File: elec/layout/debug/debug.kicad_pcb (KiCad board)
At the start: 2 copper layers, 100 x 100 mm, 100 parts

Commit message: merge
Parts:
- added C32: 10V 4.7uF X5R ±20% 0402 Multilayer Ceramic Capacitors MLCC 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, lib:C0402, F.Cu at (154.7, 68.9)
- added C33: 16V 100nF X7R ±10% 0402 Multilayer Ceramic Capacitors MLCC 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, lib:C0402, F.Cu at (163.1, 71.5)
- added C34: 25V 1uF X5R ±10% 0402 Multilayer Ceramic Capacitors MLCC - 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, lib:C0402, F.Cu at (154.7, 66.4)
- added C35: 16V 100nF X7R ±10% 0402 Multilayer Ceramic Capacitors MLCC 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, lib:C0402, F.Cu at (163.0, 70.4)
- added C36: 50V 10nF X7R ±10% 0402 Multilayer Ceramic Capacitors MLCC -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, lib:C0402, F.Cu at (154.7, 65.5)
- added C37: 50V 13pF C0G ±2% 0402 Multilayer Ceramic Capacitors MLCC - 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, lib:C0402, F.Cu at (156.3, 73.2)
- added C38: 50V 13pF C0G ±2% 0402 Multilayer Ceramic Capacitors MLCC - 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, lib:C0402, F.Cu at (154.7, 69.9)
- added C39: 50V 11pF C0G ±5% 0402 Multilayer Ceramic Capacitors MLCC - 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, lib:C0402, F.Cu at (179.4, 62.1)
- added C40: 50V 11pF C0G ±5% 0402 Multilayer Ceramic Capacitors MLCC - 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, lib:C0402, F.Cu at (174.7, 62.7)
- added C41: 10V 470nF X5R ±10% 0402 Multilayer Ceramic Capacitors MLCC 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, lib:C0402, F.Cu at (179.4, 64.1)
- added C42: 16V 100nF X7R ±10% 0402 Multilayer Ceramic Capacitors MLCC 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, lib:C0402, F.Cu at (178.3, 71.0)
- added C43: 16V 100nF X7R ±10% 0402 Multilayer Ceramic Capacitors MLCC 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, lib:C0402, F.Cu at (175.2, 68.3)
- added C44: 50V 10nF X7R ±10% 0402 Multilayer Ceramic Capacitors MLCC -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, lib:C0402, F.Cu at (175.2, 69.3)
- added C45: 50V 10nF X7R ±10% 0402 Multilayer Ceramic Capacitors MLCC -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, lib:C0402, F.Cu at (180.5, 64.1)
- added C46: 50V 1pF C0G 0402 Multilayer Ceramic Capacitors MLCC - SMD/S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, lib:C0402, F.Cu at (182.1, 68.6)
- added C47: 50V 1pF C0G 0402 Multilayer Ceramic Capacitors MLCC - SMD/S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, lib:C0402, F.Cu at (182.8, 65.7)
- added C48: 50V 1pF C0G 0402 Multilayer Ceramic Capacitors MLCC - SMD/S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, lib:C0402, F.Cu at (185.6, 65.7)
- added C49: 50V 1pF C0G 0402 Multilayer Ceramic Capacitors MLCC - SMD/S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, lib:C0402, F.Cu at (184.2, 66.2)
- added C50: 50V 100pF C0G ±5% 0402 Multilayer Ceramic Capacitors MLCC -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, lib:C0402, F.Cu at (186.0, 67.1)
- added L2: , lib:L0402, F.Cu at (182.3, 67.2)
- added L3: , lib:L0402, F.Cu at (184.2, 67.2)
- added R16: 62.5mW Thick Film Resistors ±100ppm/℃ ±1% 330Ω 0402 Chip Re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, lib:R0402, F.Cu at (158.8, 64.1)
- added R17: 62.5mW Thick Film Resistors ±100ppm/℃ ±1% 10kΩ 0402 Chip Re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, lib:R0402, F.Cu at (157.2, 64.1)
- added U12: , lib:UFQFPN-32_L5.0-W5.0-P0.50-TL-EP3.5, F.Cu at (158.9, 68.5)
- added U13: , lib:FC-135R_L3.2-W1.5, F.Cu at (154.5, 72.4)
- added U14: , lib:QFN-24_L4.0-W4.0-P0.50-BL-EP2.6, F.Cu at (178.7, 67.4)
- added U15: , lib:OSC-SMD_4P-L2.0-W1.6-BL, F.Cu at (177.0, 62.7)
- added U16: , lib:IPEX-SMD_BWIPX-1-001E, F.Cu at (188.5, 67.1)
- added U17: , lib:HDR-SMD_10P-P1.27-V-M-R2-C5-LS5.3, F.Cu at (164.6, 58.2)
- renumbered C32 to C51, C33 to C52, C34 to C53, C35 to C54, R16 to R18, R17 to R19, R18 to R20, R19 to R21, R20 to R22, R21 to R23, R22 to R24, R23 to R25, R24 to R26, R25 to R27, R26 to R28, R27 to R29, R28 to R30, R29 to R31, R30 to R32, R31 to R33, R32 to R34, R33 to R35, R34 to R36, R35 to R37, R36 to R38, R37 to R39, R38 to R40, U12 to U18, U13 to U19, U14 to U20, U15 to U21, U16 to U22, U17 to U23, U18 to U24, U19 to U25, U20 to U26, U21 to U27, U22 to U28, U23 to U29, U24 to U30
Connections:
- net vcc-13 renamed vcc-19
- net vcc-14 renamed vcc-20
- net vcc-15 renamed vcc-21
- net vcc-16 renamed vcc-22
- net vcc-17 renamed vcc-23
- R28 pad 2: _7 -> _7-1
- R32 pad 2: _7-1 -> _7-2
- R36 pad 2: _7-2 -> _7-3
- R40 pad 2: _7-3 -> _7-4
- U27 pad 7: _7 -> _7-1
- U28 pad 7: _7-1 -> _7-2
- U29 pad 7: _7-2 -> _7-3
- U30 pad 7: _7-3 -> _7-4
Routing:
- net gnd: track 85.0 -> 114.7 mm, vias 12 -> 20
- net gnd-5: track 1.55 -> 14.2 mm, vias 0 -> 43
- net pc14_osc32_in: track 0.00 -> 12.5 mm
- net vcc: track 102.0 -> 113.2 mm, vias 20 -> 24
- net vcc-15: track 0.00 -> 8.78 mm, vias 0 -> 2
- net pc15_osc32_out: track 0.00 -> 8.52 mm
- net preterm: track 0.00 -> 6.08 mm
- net vcc-7: track 23.4 -> 28.1 mm
- net vcc-18: track 0.00 -> 2.86 mm
- net vcc-17: track 0.00 -> 2.86 mm
- net io-3: track 0.00 -> 2.28 mm
- net _7: track 2.28 -> 0.00 mm
- net _7-4: track 0.00 -> 2.28 mm
- net ph3_boot0: track 0.00 -> 1.62 mm
- net vcc-1: track 78.4 -> 79.9 mm
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
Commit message: layout 95%
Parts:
- added C55: 25V 1uF X5R ±10% 0402 Multilayer Ceramic Capacitors MLCC - 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, lib:C0402, F.Cu at (173.8, 102.9)
- added C56: 25V 1uF X5R ±10% 0402 Multilayer Ceramic Capacitors MLCC - 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, lib:C0402, F.Cu at (175.7, 102.9)
- added R41: 62.5mW Thick Film Resistors ±100ppm/℃ ±1% 1kΩ 0402 Chip Res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, lib:R0402, F.Cu at (160.1, 83.3)
- added R42: 62.5mW Thick Film Resistors ±100ppm/℃ ±1% 1kΩ 0402 Chip Res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, lib:R0402, F.Cu at (157.5, 83.3)
- added R43: 62.5mW Thick Film Resistors ±100ppm/℃ ±1% 1kΩ 0402 Chip Res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, lib:R0402, F.Cu at (155.0, 83.3)
- added R44: 62.5mW Thick Film Resistors ±100ppm/℃ ±1% 1kΩ 0402 Chip Res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, lib:R0402, F.Cu at (152.4, 83.3)
- added R45: 62.5mW Thick Film Resistors ±100ppm/℃ ±1% 1kΩ 0402 Chip Res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, lib:R0402, F.Cu at (168.9, 61.2)
- added R46: 62.5mW Thick Film Resistors ±100ppm/℃ ±1% 1kΩ 0402 Chip Res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, lib:R0402, F.Cu at (171.4, 61.2)
- added R47: 62.5mW Thick Film Resistors ±100ppm/℃ ±1% 1kΩ 0402 Chip Res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, lib:R0402, F.Cu at (174.0, 61.2)
- added R48: 62.5mW Thick Film Resistors ±100ppm/℃ ±1% 1kΩ 0402 Chip Res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, lib:R0402, F.Cu at (176.5, 61.2)
- added U27: , lib:VSSOP-10_L3.0-W3.0-P0.50-LS4.9-BL, F.Cu at (174.9, 105.1)
- added U28: , lib:CONN-TH_DB125-2.54-2P-GN, F.Cu at (195.8, 106.0)
- added U33: , lib:HDR-SMD_8P-P2.54-V-M-R2-C4-LS7.4, F.Cu at (156.2, 88.9)
- added U34: , lib:HDR-SMD_8P-P2.54-V-M-R2-C4-LS7.4, F.Cu at (172.7, 55.6)
- moved C44 6.14 mm to (171.8, 74.4)
- moved C42 5.78 mm to (174.6, 75.4)
- moved C32 5.58 mm to (151.3, 73.4)
- moved C33 5.58 mm to (159.7, 76.0)
- moved C34 5.58 mm to (151.3, 70.9)
- moved C35 5.58 mm to (159.7, 74.9)
- moved C38 5.58 mm to (151.3, 74.4)
- moved C39 5.58 mm to (176.1, 66.6)
- moved C40 5.58 mm to (171.4, 67.1)
- moved C41 5.58 mm to (176.1, 68.6)
- moved C45 5.58 mm to (177.1, 68.6)
- moved C46 5.58 mm to (178.7, 73.1)
- moved C47 5.58 mm to (179.4, 70.2)
- moved C49 5.58 mm to (180.8, 70.7)
- moved L2 5.58 mm to (178.9, 71.6)
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- renumbered U27 to U29, U28 to U30, U29 to U31, U30 to U32
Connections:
- net vcc-20 renamed vcc-24
- C39 pad 1: xin-1 -> xta
- C40 pad 1: xout-1 -> xtb
- C41 pad 1: vcc-15 -> vcc-19
- C44 pad 1: vcc-15 -> vcc-19
- C45 pad 1: vcc-14 -> vcc-18
- C46 pad 1: io-3 -> io-1
- C47 pad 1: vcc-17 -> vcc-21
- C48 pad 1: vcc-18 -> vcc-22
- C49 pad 1: vcc-17 -> vcc-21
- C49 pad 2: vcc-18 -> vcc-22
- C50 pad 1: vcc-18 -> vcc-22
- C50 pad 2: gnd-11 -> gnd-10
- L2 pad 1: io-3 -> io-1
- L2 pad 2: vcc-17 -> vcc-21
- L3 pad 1: vcc-17 -> vcc-21
- L3 pad 2: vcc-18 -> vcc-22
- R24 pad 2: vcc-19 -> vcc-23
- R40 pad 1: vcc-23 -> vcc-28
- U12 pad 18: io -> vcc-13
- U12 pad 19: scl-1 -> vcc-14
- U12 pad 20: sda-1 -> vcc-15
- U12 pad 21: io-1 -> vcc-16
- U12 pad 27: io-2 -> io
- U14 pad 1: vcc-14 -> vcc-18
- U14 pad 10: io -> vcc-13
- U14 pad 12: vcc-15 -> vcc-19
- U14 pad 2: vcc-15 -> vcc-19
- U14 pad 22: io-3 -> io-1
- U14 pad 3: io-2 -> io
- U14 pad 7: io-1 -> vcc-16
- U14 pad 8: sda-1 -> vcc-15
- U14 pad 9: scl-1 -> vcc-14
- U15 pad 1: xin-1 -> xta
- U15 pad 2: gnd-10 -> gnd
- U15 pad 3: xout-1 -> xtb
- U15 pad 4: gnd-10 -> gnd
- U16 pad 1: gnd-11 -> gnd-10
- U17 pad 1: vcc-13 -> vcc-17
- U20 pad 2: vcc-21 -> vcc-25
- U21 pad 2: vcc-22 -> vcc-26
- U21 pad 4: vcc-21 -> vcc-25
- U26 pad 3: vcc-19 -> vcc-23
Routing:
- net vcc-2: track 50.2 -> 148.8 mm, vias 0 -> 4
- net vcc-3: track 36.0 -> 103.1 mm
- net scl: track 41.1 -> 106.5 mm, vias 4 -> 6
- net sda: track 39.9 -> 101.2 mm
- net vcc-1: track 79.9 -> 134.1 mm, vias 4 -> 6
- net gnd: track 114.7 -> 164.2 mm, vias 20 -> 23
- net dm: track 2.76 -> 51.1 mm, vias 0 -> 4
- net dp: track 2.76 -> 47.3 mm
- net mosi-1: track 0.00 -> 36.4 mm, vias 0 -> 2
- net cs-2: track 0.00 -> 35.3 mm
- net sck-2: track 0.00 -> 32.8 mm, vias 0 -> 2
- net vcc-13: track 0.00 -> 32.4 mm, vias 0 -> 2
- net miso-2: track 0.00 -> 31.3 mm, vias 0 -> 3
- net vcc-16: track 0.00 -> 30.3 mm
- net vcc-14: track 1.18 -> 31.3 mm, vias 0 -> 2
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- added copper zone on F.Cu, net gnd
- added copper zone on In1.Cu, net gnd
- added copper zone on B.Cu, net vcc
- added copper zone on In2.Cu, net vcc
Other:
- copper layers 2 -> 4

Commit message: layout complete
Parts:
- added D1: , lib:SMA_L4.2-W2.6-LS5.3-RD, F.Cu at (119.7, 75.0)
- added J1: , lib:CONN-SMD_4P-P1.00_SM04B-SRSS-TB-LF-SN, F.Cu at (195.8, 83.5)
- added R1: 62.5mW Thick Film Resistors ±100ppm/℃ ±1% 10kΩ 0402 Chip Re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, lib:R0402, F.Cu at (181.1, 96.5)
- added R2: 62.5mW Thick Film Resistors ±100ppm/℃ ±1% 10kΩ 0402 Chip Re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, lib:R0402, F.Cu at (179.0, 97.2)
- added U37: , lib:RES-ADJ-TH_RK09K1130AJ3, F.Cu at (148.8, 139.6)
- added U4: , lib:KEY-SMD_4P-L4.2-W3.2-P2.20-LS4.6, F.Cu at (149.5, 124.8)
- added U5: , lib:KEY-SMD_4P-L4.2-W3.2-P2.20-LS4.6, F.Cu at (128.9, 116.2)
- R11: renamed from R9; value 62.5mW Thick Film Resistors ±100ppm/℃ ±1% 1MΩ 0402 Chip Resistor - Surface Mount ROHS -> 100mW Thick Film Resistors ±5% ±200ppm/℃ 1.1MΩ 0402 Chip Resistor - Surface Mount ROHS
- moved C41 2.21 mm to (177.1, 66.6)
- moved C45 2.18 mm to (178.0, 66.6)
- moved C15 0.84 mm to (124.5, 69.9)
- moved C16 0.75 mm to (122.6, 69.9)
- moved C44 0.12 mm to (171.9, 74.5)
- moved C42 0.10 mm to (174.5, 75.4)
- renumbered R8 to R10, R10 to R12, R11 to R13, R12 to R14, R13 to R15, R14 to R16, R15 to R17, R16 to R18, R17 to R19, R18 to R20, R19 to R21, R20 to R22, R21 to R23, R22 to R24, R23 to R25, R24 to R26, R25 to R27, R26 to R28, R27 to R29, R1 to R3, R28 to R30, R29 to R31, R30 to R32, R31 to R33, R32 to R34, R33 to R35, R34 to R36, R35 to R37, R36 to R38, R37 to R39, R2 to R4, R38 to R40, R39 to R41, R40 to R42, R41 to R43, R42 to R44, R43 to R45, R44 to R46, R45 to R47, R46 to R48, R47 to R49, R3 to R5, R48 to R50, R4 to R6, R5 to R7, R6 to R8, R7 to R9, U8 to U10, U9 to U11, U10 to U12, U11 to U13, U12 to U14, U13 to U15, U14 to U16, U15 to U17, U16 to U18, U17 to U19, U18 to U20, U19 to U21, U20 to U22, U21 to U23, U22 to U24, U23 to U25, U24 to U26, U25 to U27, U26 to U28, U27 to U29, U28 to U30, U29 to U31, U30 to U32, U31 to U33, U32 to U34, U33 to U35, U34 to U36, U4 to U6, U5 to U7, U6 to U8, U7 to U9
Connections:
- net vcc-28 renamed vcc-29
- C10 pad 1: vcc-7 -> vcc-8
- C11 pad 1: vcc-7 -> vcc-8
- C12 pad 1: vcc-7 -> vcc-8
- C13 pad 1: vcc-8 -> vcc-9
- C14 pad 1: vcc-9 -> vcc-10
- C15 pad 1: vcc-9 -> vcc-10
- C16 pad 1: vcc-9 -> vcc-10
- C17 pad 1: vcc-12 -> vcc-13
- C18 pad 1: vcc-12 -> vcc-13
- C20 pad 1: vcc-12 -> vcc-13
- C41 pad 1: vcc-19 -> vcc-20
- C44 pad 1: vcc-19 -> vcc-20
- C45 pad 1: vcc-18 -> vcc-19
- C46 pad 1: io-1 -> io-2
- C47 pad 1: vcc-21 -> vcc-22
- C48 pad 1: vcc-22 -> vcc-23
- C49 pad 1: vcc-21 -> vcc-22
- C49 pad 2: vcc-22 -> vcc-23
- C50 pad 1: vcc-22 -> vcc-23
- C9 pad 1: vcc-7 -> vcc-8
- L2 pad 1: io-1 -> io-2
- L2 pad 2: vcc-21 -> vcc-22
- L3 pad 1: vcc-21 -> vcc-22
- L3 pad 2: vcc-22 -> vcc-23
- LED1 pad 2: vcc-9 -> vcc-10
- LED2 pad 2: vcc-9 -> vcc-10
- R11 pad 1: vcc-12 -> vcc-13
- R18 pad 1: vcc-1 -> vcc-2
- R26 pad 2: vcc-23 -> vcc-7
- R40 pad 1: vcc-8 -> vcc-9
- R41 pad 1: vcc-9 -> vcc-10
- R47 pad 1: vcc-15 -> vcc-16
- R48 pad 1: vcc-14 -> vcc-15
- R49 pad 1: vcc-13 -> vcc-14
- R50 pad 1: vcc-16 -> vcc-17
- U1 pad 23: vcc-7 -> vcc-8
- U1 pad 35: gpio23 -> io
- U1 pad 38: gpio26_a0 -> vcc-7
- U1 pad 45: vcc-7 -> vcc-8
- U1 pad 50: vcc-7 -> vcc-8
- U14 pad 18: vcc-13 -> vcc-14
- U14 pad 19: vcc-14 -> vcc-15
- U14 pad 20: vcc-15 -> vcc-16
- U14 pad 21: vcc-16 -> vcc-17
- U14 pad 27: io -> io-1
- U14 pad 29: vcc-1 -> vcc-2
- U14 pad 30: vcc-2 -> vcc-1
- U16 pad 1: vcc-18 -> vcc-19
- U16 pad 10: vcc-13 -> vcc-14
- U16 pad 12: vcc-19 -> vcc-20
- U16 pad 2: vcc-19 -> vcc-20
- U16 pad 22: io-1 -> io-2
- U16 pad 3: io -> io-1
- U16 pad 7: vcc-16 -> vcc-17
- U16 pad 8: vcc-15 -> vcc-16
- U16 pad 9: vcc-14 -> vcc-15
- U19 pad 1: vcc-17 -> vcc-18
- U20 pad A4: vcc-8 -> vcc-9
- U20 pad A9: vcc-8 -> vcc-9
- U20 pad B4: vcc-8 -> vcc-9
- U20 pad B9: vcc-8 -> vcc-9
- U21 pad 2: vcc-24 -> vcc-25
- U22 pad 2: vcc-25 -> vcc-26
- U22 pad 4: vcc-24 -> vcc-25
- U23 pad 2: vcc-26 -> vcc-27
- U23 pad 4: vcc-25 -> vcc-26
- U28 pad 3: vcc-23 -> vcc-7
- U6 pad 2: vcc-9 -> vcc-10
- U7 pad 1: vcc-8 -> vcc-9
- U7 pad 10: vcc-9 -> vcc-10
- U7 pad 7: vcc-8 -> vcc-9
- U8 pad 10: vcc-9 -> vcc-10
- U8 pad 11: vcc-9 -> vcc-10
- U8 pad 4: vcc-12 -> vcc-13
- U8 pad 5: vcc-12 -> vcc-13
- U9 pad 3: vcc-12 -> vcc-13
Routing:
- net vcc-10: track 0.00 -> 51.9 mm
- net gnd: track 164.2 -> 211.0 mm, vias 23 -> 65
- net vcc-7: track 23.4 -> 60.5 mm
- net vcc-17: track 0.00 -> 30.3 mm
- net vcc-9: track 35.2 -> 65.1 mm, vias 0 -> 2
- net io-1: track 2.28 -> 31.5 mm, vias 0 -> 2
- net io: track 0.00 -> 27.7 mm, vias 0 -> 1
- net vcc-8: track 50.3 -> 23.4 mm
- net vcc-12: track 23.2 -> 0.00 mm
- net run: track 0.00 -> 19.7 mm, vias 0 -> 2
- net sda: track 101.2 -> 113.7 mm, vias 4 -> 5
- net vcc-20: track 0.00 -> 11.7 mm, vias 0 -> 2
- net vina: track 1.41 -> 12.1 mm, vias 0 -> 2
- net vcc-26: track 0.00 -> 9.41 mm
- net vcc-24: track 9.41 -> 0.00 mm
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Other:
- board text added: "3v3"
- board text added: "AMS1117-3V3 LDO"
- board text added: "BATT"
- board text added: "BMI088"
- board text added: "BNO055"
- board text added: "CS"
- board text added: "DRV2605"
- board text added: "GND"
- board text added: "GPIO26"
- board text added: "HAPTIC"
- board text added: "IMU Interrupt"
- board text added: "LED1"
- board text added: "LED2"
- board text added: "LED3"
- board text added: "LED_din"
- board text added: "LIS3MD"
- board text added: "MENU1"
- board text added: "MENU2"
- board text added: "MENU3"
- board text added: "MISO"
- board text added: "MOSI"
- board text added: "PWR"
- board text added: "SCK"
- board text added: "STM32L4"
- board text added: "TPS6300 BUCK"
- board text added: "USB_DM"
- board text added: "USB_DP"
- board text added: "VBATT"
- board text added: "VUSB"

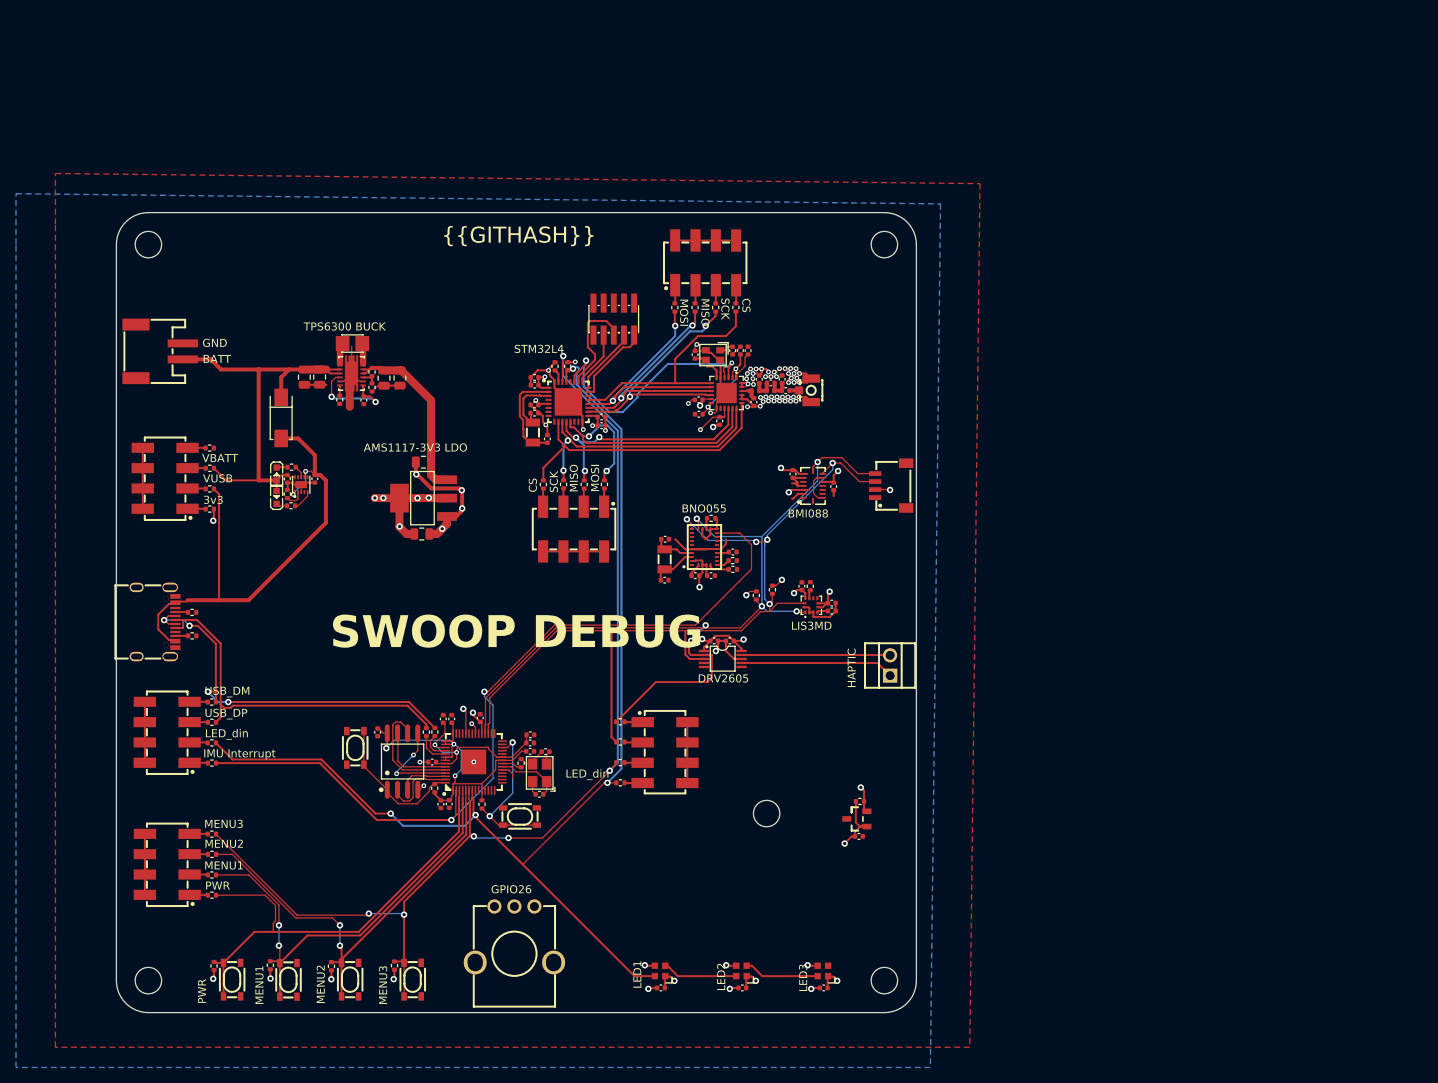
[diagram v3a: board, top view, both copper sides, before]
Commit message: added equation support
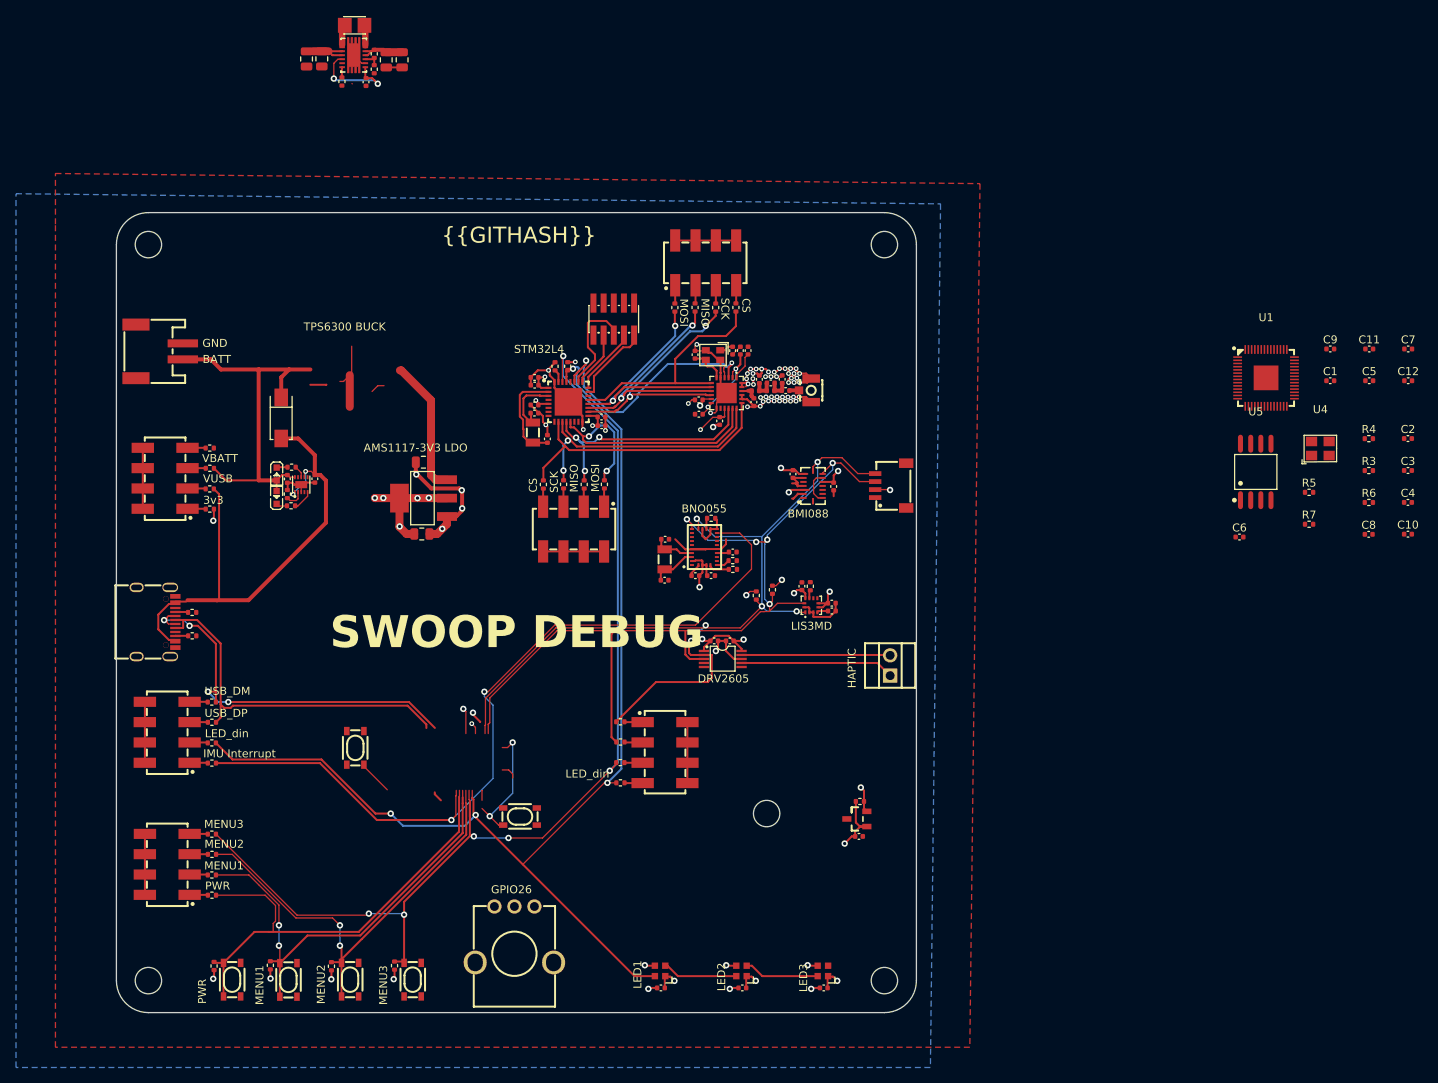
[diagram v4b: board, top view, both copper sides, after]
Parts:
- removed the U2 at (152.0, 119.4)
- removed the U3 at (134.8, 118.0)
- added U4: , lib:OSC-SMD_4P-L3.2-W2.5-BL, F.Cu at (249.6, 78.8)
- added U5: , lib:SOIC-8_L5.3-W5.3-P1.27-LS8.0-BL, F.Cu at (241.5, 81.8)
- R3: value 62.5mW Thick Film Resistors ±100ppm/℃ ±1% 1kΩ 0402 Chip Resistor - Surface Mount ROHS -> 62.5mW Thick Film Resistors ±100ppm/℃ ±1% 10kΩ 0402 Chip Resistor - Surface Mount ROHS
- R4: value 62.5mW Thick Film Resistors ±100ppm/℃ ±1% 27kΩ 0402 Chip Resistor - Surface Mount ROHS -> 62.5mW Thick Film Resistors ±100ppm/℃ ±1% 10kΩ 0402 Chip Resistor - Surface Mount ROHS
- R5: value 62.5mW Thick Film Resistors ±100ppm/℃ ±1% 27kΩ 0402 Chip Resistor - Surface Mount ROHS -> 62.5mW Thick Film Resistors ±100ppm/℃ ±1% 1kΩ 0402 Chip Resistor - Surface Mount ROHS
- R6, R7: value 62.5mW Thick Film Resistors ±100ppm/℃ ±1% 10kΩ 0402 Chip Resistor - Surface Mount ROHS -> 62.5mW Thick Film Resistors ±100ppm/℃ ±1% 27kΩ 0402 Chip Resistor - Surface Mount ROHS
- moved C5 127.5 mm to (255.7, 70.4), turned to 0 degrees
- moved C8 126.3 mm to (255.6, 89.6), turned to 0 degrees
- moved C7 124.8 mm to (260.5, 66.4), turned to 0 degrees
- moved C9 123.6 mm to (250.8, 66.4), turned to 0 degrees
- moved R4 123.4 mm to (255.6, 77.6), turned to 0 degrees
- moved C10 122.8 mm to (260.5, 89.5), turned to 0 degrees
- moved C4 122.6 mm to (260.5, 85.6), turned to 0 degrees
- moved C12 118.3 mm to (260.5, 70.4)
- moved R6 117.1 mm to (255.6, 85.6), turned to 0 degrees
- moved C11 115.9 mm to (255.7, 66.4)
- moved C3 115.2 mm to (260.5, 81.6)
- moved C2 114.7 mm to (260.5, 77.6)
- moved R7 114.2 mm to (248.1, 88.3), turned to 0 degrees
- moved R5 113.3 mm to (248.1, 84.3), turned to 0 degrees
- moved R3 112.1 mm to (255.6, 81.6), turned to 0 degrees
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- renumbered U4 to U2, U5 to U3
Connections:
- net cs-2 renamed cs-3
- R3 pad 1: xout -> vcc
- R3 pad 2: out -> run
- R4 pad 1: usb_dp -> vcc
- R4 pad 2: dp -> cs-1
- R5 pad 1: dm -> xout
- R5 pad 2: usb_dm -> out
- R6 pad 1: vcc -> dp
- R6 pad 2: run -> dp
- R7 pad 1: vcc -> dm
- R7 pad 2: cs -> dm
- U1 pad 12: gpio9 -> cs
- U1 pad 13: sck-1 -> sck
- U1 pad 43: vcc -> adc_avdd
- U1 pad 46: usb_dm -> dm
- U1 pad 47: usb_dp -> dp
- U1 pad 48: vcc -> usb_vdd
- U1 pad 52: sck -> sck-1
- U1 pad 56: cs -> cs-1
- U3 pad 1: cs -> cs-1
- U3 pad 2: cs -> cs-1
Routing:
- net vcc: track 136.9 -> 94.4 mm, vias 35 -> 32
- net vcc-8: track 23.4 -> 0.00 mm, vias 2 -> 0
- net cs: track 18.1 -> 0.00 mm
- net sck: track 14.4 -> 0.00 mm
- net io0: track 12.8 -> 0.00 mm, vias 2 -> 0
- net io3: track 9.73 -> 0.00 mm
- net io1: track 9.57 -> 0.00 mm
- net xin: track 8.08 -> 0.00 mm
- net io2: track 6.20 -> 0.00 mm
- net gnd: track 211.0 -> 205.6 mm, vias 65 -> 62
- net cs-1: track 0.00 -> 4.35 mm
- net run: track 19.7 -> 15.5 mm
- net vcc-1: track 141.0 -> 136.8 mm
- net usb_dp: track 4.15 -> 0.00 mm
- net out: track 3.72 -> 0.00 mm
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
